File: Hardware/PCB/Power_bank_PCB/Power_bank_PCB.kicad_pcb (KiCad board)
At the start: 2 copper layers, 94 parts, among them IC1 TPS63070RNMR, IC2 TPS63070RNMR, J1 Alterative_charging, J2 Vout, Q1 2N7002, Q2 8205A, Q3 2N7002, Q4 2N7002, Q5 2N7002, Q6 DMP3099L, U1 TP4056-42-ESOP8, U2 MCP4018-10k, U3 DW01A, U4 TPS61022, U5 STM32U031F8Px, U6 INA219AxD

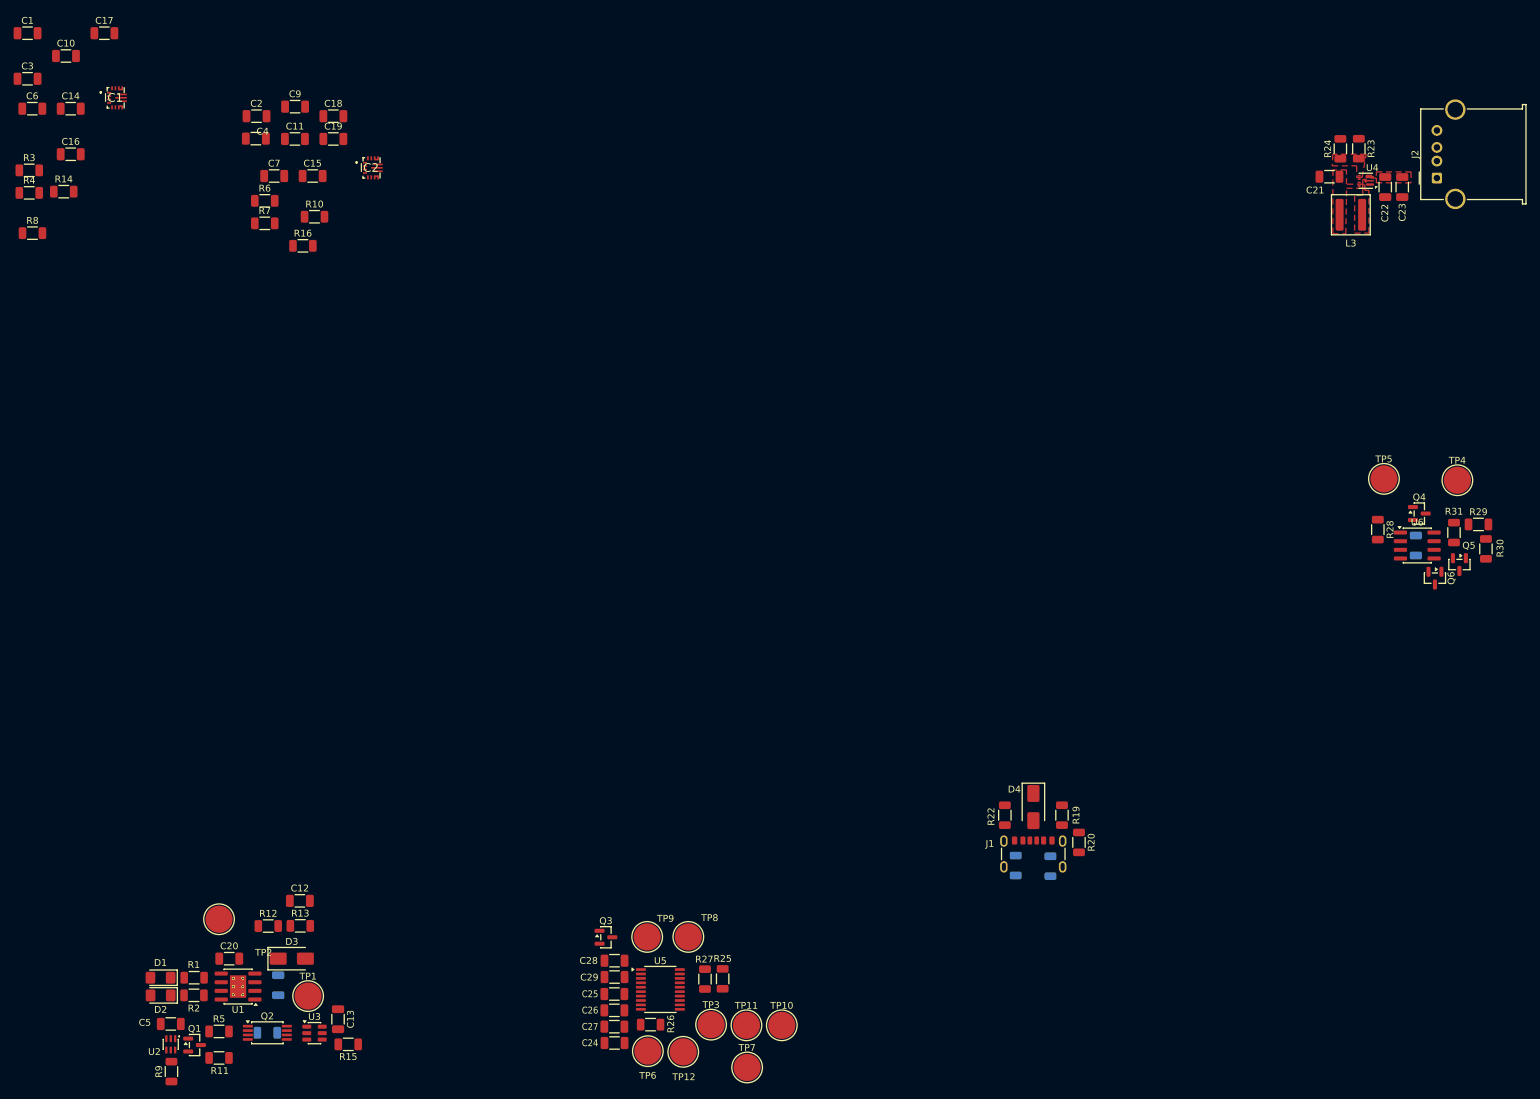
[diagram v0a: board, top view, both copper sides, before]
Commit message: First layout without traces
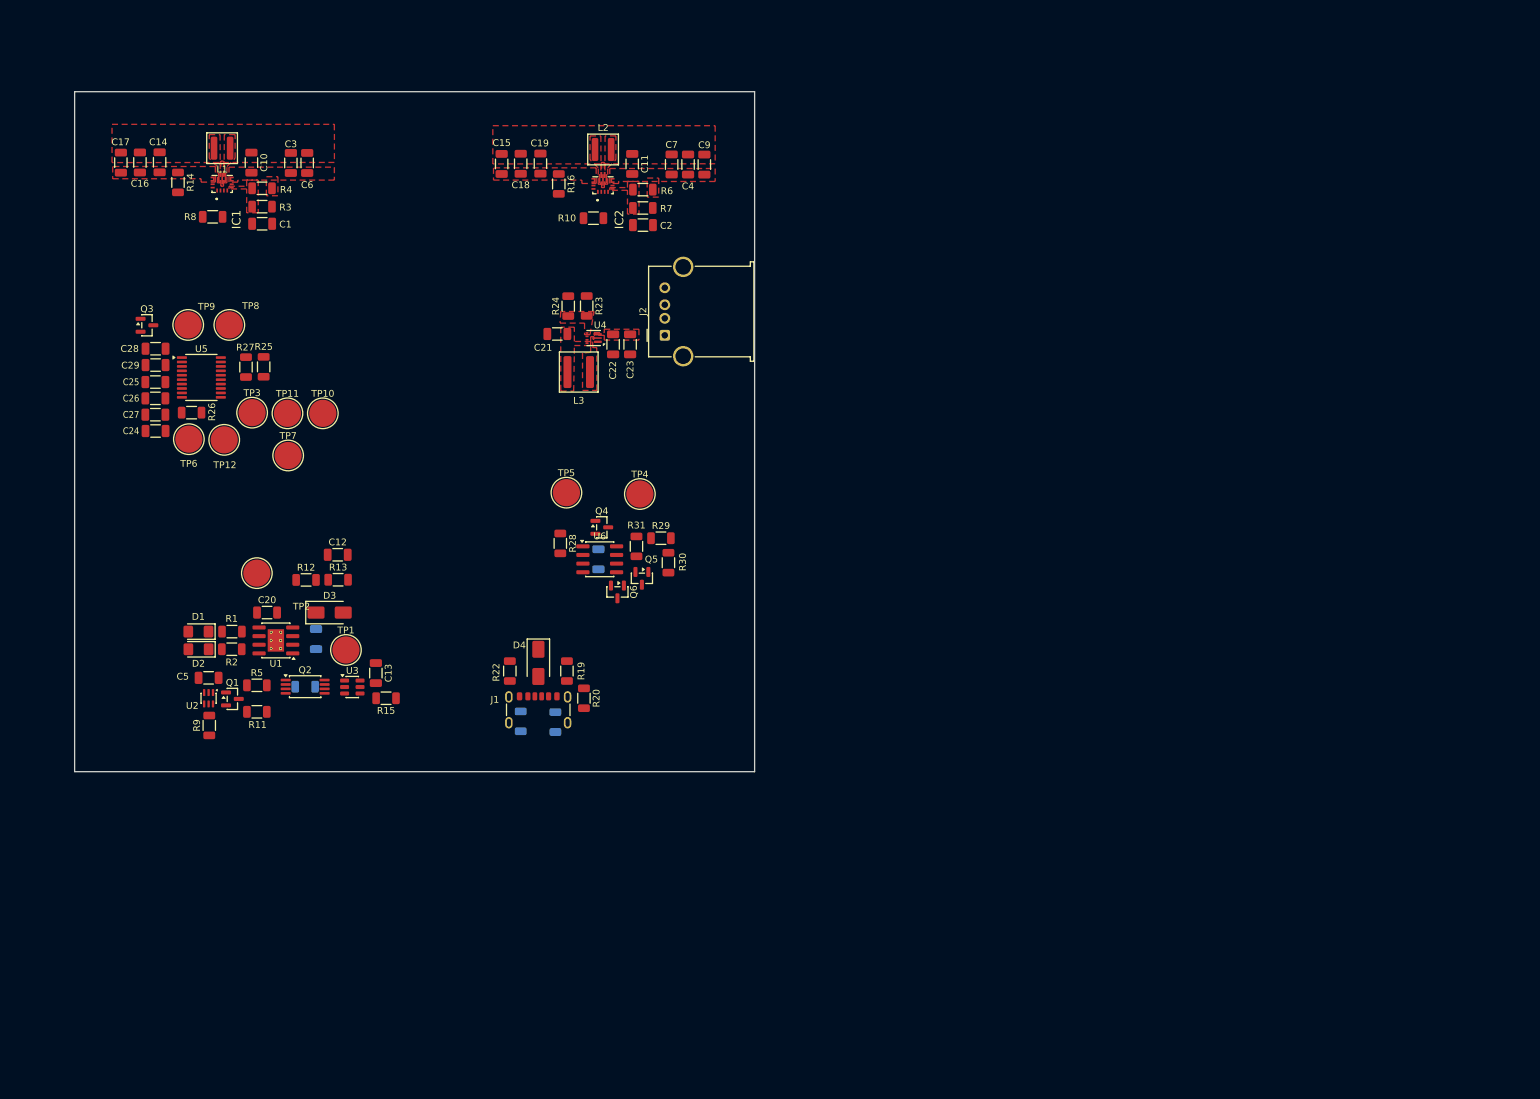
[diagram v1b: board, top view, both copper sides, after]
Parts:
- added L1: 1.5uH / XFL4020, Inductor_SMD:L_Coilcraft_XAL4020-XXX, F.Cu at (64.0, 45.1)
- added L2: 1.5uH / XFL4020, Inductor_SMD:L_Coilcraft_XAL4020-XXX, F.Cu at (120.0, 45.3)
- moved C30 120.2 mm to (119.3, 105.6)
- moved Q4 120.2 mm to (119.8, 100.9)
- moved R31 120.2 mm to (124.9, 103.7)
- moved TP4 120.2 mm to (125.4, 96.0)
- moved Q5 120.2 mm to (125.7, 108.4)
- moved Q6 120.2 mm to (122.1, 110.4)
- moved R28 120.2 mm to (113.7, 103.2)
- moved R29 120.2 mm to (128.5, 102.5)
- moved R30 120.2 mm to (129.6, 106.1)
- moved TP5 120.2 mm to (114.6, 95.8)
- moved U6 120.2 mm to (119.5, 105.6)
- moved L3 115.9 mm to (116.4, 78.0)
- moved C21 115.9 mm to (113.3, 72.4)
- moved C22 115.9 mm to (121.5, 74.0)
- moved C23 115.9 mm to (124.0, 74.0)
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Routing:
- added copper zone on F.Cu, net +3.3V
- added copper zone on F.Cu, net GND
- added copper zone on F.Cu, net Net-(IC1-FB)
- added copper zone on F.Cu, net Net-(IC1-L1)
- added copper zone on F.Cu, net Net-(IC1-L2)
- added copper zone on F.Cu, net Net-(IC2-FB)
- added copper zone on F.Cu, net Net-(IC2-L1)
- added copper zone on F.Cu, net Net-(IC2-L2)
- added copper zone on F.Cu, net Vcharge
- added copper zone on F.Cu, net Vfoto
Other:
- board outline added: 100 x 100 mm

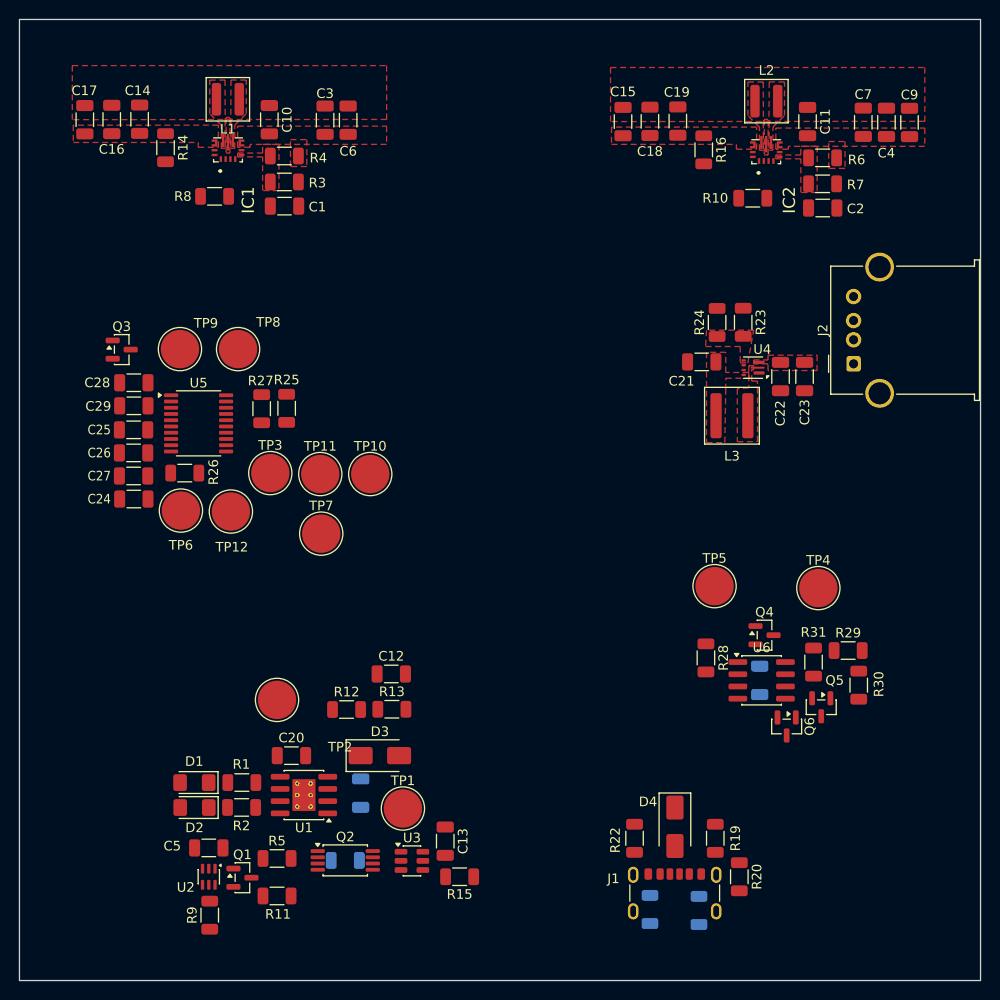
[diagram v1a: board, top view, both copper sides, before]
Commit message: Positioned modules on PCB and created zones
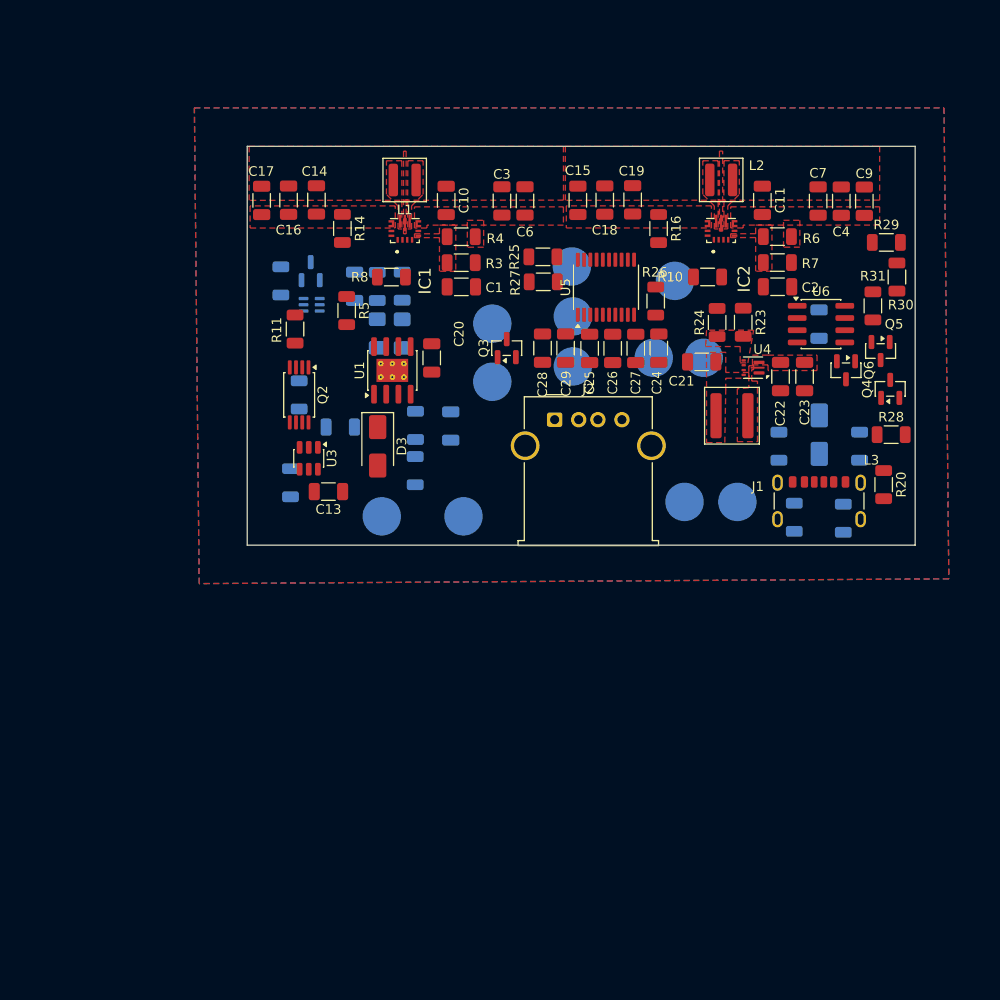
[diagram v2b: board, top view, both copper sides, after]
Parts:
- C12, C5, D1, D2, D4, Q1, R1, R12, R13, R15, R19, R2, R22, R9, TP1, TP10, TP11, TP12, TP2, TP3, TP4, TP5, TP6, TP7, TP8, TP9, U2: moved to B.Cu
- moved R9 66.4 mm to (69.5, 64.0), turned to -90 degrees
- moved Q1 63.5 mm to (72.6, 63.0), turned to 90 degrees
- moved U2 60.5 mm to (72.7, 66.5), turned to 180 degrees
- moved C5 60.4 mm to (77.2, 64.6), turned to -90 degrees
- moved R11 59.0 mm to (71.0, 69.0), turned to -90 degrees
- moved R5 57.5 mm to (76.3, 67.1), turned to -90 degrees
- moved C24 56.8 mm to (108.8, 71.0), turned to 90 degrees
- moved R2 56.0 mm to (79.5, 64.6), turned to 90 degrees
- moved R1 54.3 mm to (82.1, 64.5), turned to 90 degrees
- moved C27 53.9 mm to (106.4, 71.0), turned to 90 degrees
- moved D2 52.9 mm to (79.5, 69.5), turned to -90 degrees
- moved R26 52.2 mm to (108.5, 66.1), turned to 90 degrees
- moved TP12 52.1 mm to (110.5, 64.0), turned to 90 degrees
- moved TP6 51.7 mm to (108.3, 72.0), turned to 90 degrees
- moved D1 51.5 mm to (82.1, 69.5), turned to -90 degrees
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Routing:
- added copper zone on B.Cu, net GND
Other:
- board size 100 x 100 mm -> 69.5 x 41.5 mm

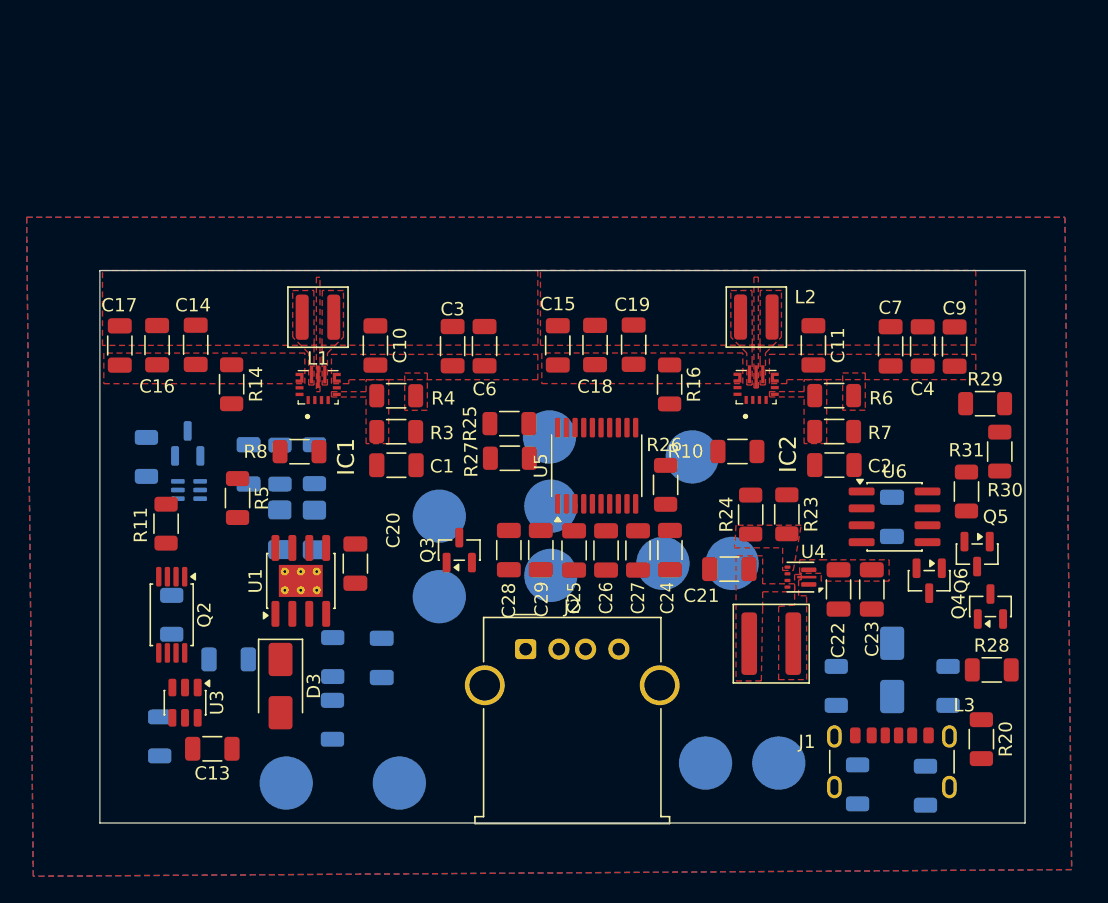
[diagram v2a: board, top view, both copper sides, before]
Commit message: Generic PCB layout done,
need some polish and fix minor 25+ DRC errors
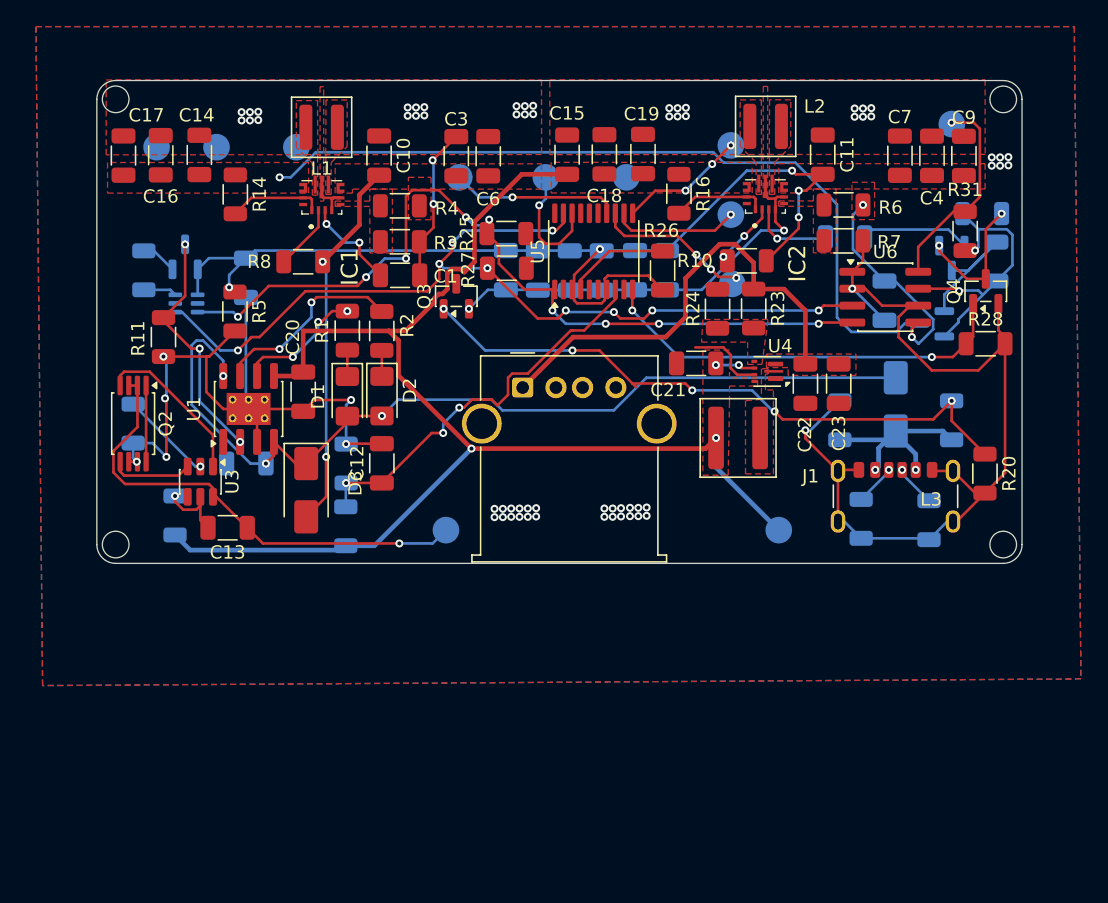
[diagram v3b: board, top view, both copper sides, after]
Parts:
- C12, D1, D2, R1, R2: moved to F.Cu
- C2, C24, C25, C26, C27, C28, C29, Q5, Q6, R29, R30: moved to B.Cu
- TP1, TP10, TP11, TP12, TP2, TP3, TP4, TP5, TP6, TP7, TP8, TP9: footprint TestPoint:TestPoint_Pad_D4.0mm -> TestPoint:TestPoint_Pad_D2.0mm
- moved TP5 59.1 mm to (74.8, 40.7)
- moved TP7 53.4 mm to (70.3, 40.7)
- moved TP4 49.7 mm to (130.0, 39.0), turned to 180 degrees
- moved TP6 41.7 mm to (80.8, 40.7)
- moved TP10 35.0 mm to (113.4, 40.6), turned to 90 degrees
- moved TP8 34.5 mm to (105.5, 43.0), turned to 90 degrees
- moved TP2 34.3 mm to (117.0, 69.5)
- moved TP12 27.3 mm to (93.0, 43.0)
- moved TP9 26.7 mm to (99.5, 43.0), turned to 90 degrees
- moved TP11 25.7 mm to (113.4, 45.8), turned to 90 degrees
- moved R28 24.5 mm to (132.5, 55.5)
- moved C24 24.4 mm to (96.5, 50.0)
- moved C28 24.1 mm to (108.6, 50.0)
- moved Q4 23.7 mm to (132.6, 51.6)
- moved TP1 22.5 mm to (92.0, 69.5)
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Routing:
- net GND: track 0.00 -> 183.1 mm, vias 0 -> 72
- net Vbat: track 0.00 -> 100.8 mm, vias 0 -> 4
- net +3.3V: track 0.00 -> 93.2 mm, vias 0 -> 7
- net /SDA: track 0.00 -> 69.7 mm, vias 0 -> 9
- net Vbus: track 0.00 -> 69.0 mm, vias 0 -> 3
- net /SCL: track 0.00 -> 62.3 mm, vias 0 -> 9
- net Vfoto: track 0.00 -> 59.7 mm, vias 0 -> 1
- net /USB_FLAG: track 0.00 -> 47.6 mm, vias 0 -> 5
- net /Bat-: track 0.00 -> 35.9 mm, vias 0 -> 1
- net /5V: track 0.00 -> 34.6 mm
- net /Fotopanel_disable: track 0.00 -> 31.7 mm, vias 0 -> 2
- net /Battery_state: track 0.00 -> 30.0 mm, vias 0 -> 3
- net Vcharge: track 0.00 -> 28.1 mm, vias 0 -> 2
- net Net-(Q6-S): track 0.00 -> 20.9 mm, vias 0 -> 2
- net Net-(Q1-D): track 0.00 -> 18.3 mm, vias 0 -> 3
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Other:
- board size 69.5 x 41.5 mm -> 69.5 x 36.3 mm

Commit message: Update of PCB layout
moved battery state resistors close to STM32
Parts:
- moved R12 15.4 mm to (91.4, 55.5), turned to 0 degrees
- moved R13 14.7 mm to (96.1, 55.5), turned to 0 degrees
- moved C12 9.65 mm to (92.6, 56.5)
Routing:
- net /Battery_state: track 30.0 -> 21.4 mm, vias 3 -> 1
- net GND: track 183.1 -> 186.2 mm, vias 72 -> 70
- net Vbat: track 100.8 -> 101.8 mm, vias 4 -> 5
- net /USB_FLAG: track 47.6 -> 48.4 mm

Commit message: Further layout update
Minor fixes
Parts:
- moved U3 0.40 mm to (73.2, 65.9)
- moved C21 0.32 mm to (110.8, 57.3)
- moved L2 0.23 mm to (116.0, 39.4)
- moved L1 0.21 mm to (82.7, 39.4)
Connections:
- IC1 pad 16: (no net) -> Vfoto
- IC1 pad 17: (no net) -> Vcharge
- IC2 pad 16: (no net) -> Vbat
- IC2 pad 17: (no net) -> +3.3V
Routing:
- net GND: track 186.2 -> 219.4 mm, vias 70 -> 73
- net Net-(Q3-D): track 7.78 -> 19.5 mm, vias 0 -> 2
- net Net-(U5-PA13): track 0.00 -> 6.75 mm, vias 0 -> 1
- net /Bat-: track 35.9 -> 41.8 mm
- net +3.3V: track 93.2 -> 97.7 mm, vias 7 -> 8
- net Net-(J2-D+): track 0.00 -> 2.00 mm
- net Net-(U3-CS): track 6.99 -> 7.92 mm
- net Net-(U6-IN+): track 15.5 -> 16.1 mm
- net /SCL: track 62.3 -> 62.1 mm, vias 9 -> 11
- net Vcharge: track 28.1 -> 28.3 mm, vias 2 -> 4
- net Net-(U1-~{STDBY}): vias 3 -> 2

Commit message: Solved minor DRC warnings
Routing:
- net GND: track 219.4 -> 245.7 mm, vias 73 -> 77
- net Net-(IC2-FB): track 0.00 -> 5.74 mm
- net Net-(IC1-FB): track 0.00 -> 5.74 mm
- removed copper zone on F.Cu, net Net-(IC1-FB)
- removed copper zone on F.Cu, net Net-(IC2-FB)
